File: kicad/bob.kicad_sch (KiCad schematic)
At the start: 49 parts, among them J1 GPIO (Optional), J2 Mini USB Female, J3 Battery Connector, J4 GPIO (Optional), SW1 Screw Switch, U1 RP2040, U2 W25Q64JVSS, U3 NCP1117-3.3_SOT223, U4 MPU-6050, Y1 12MHz

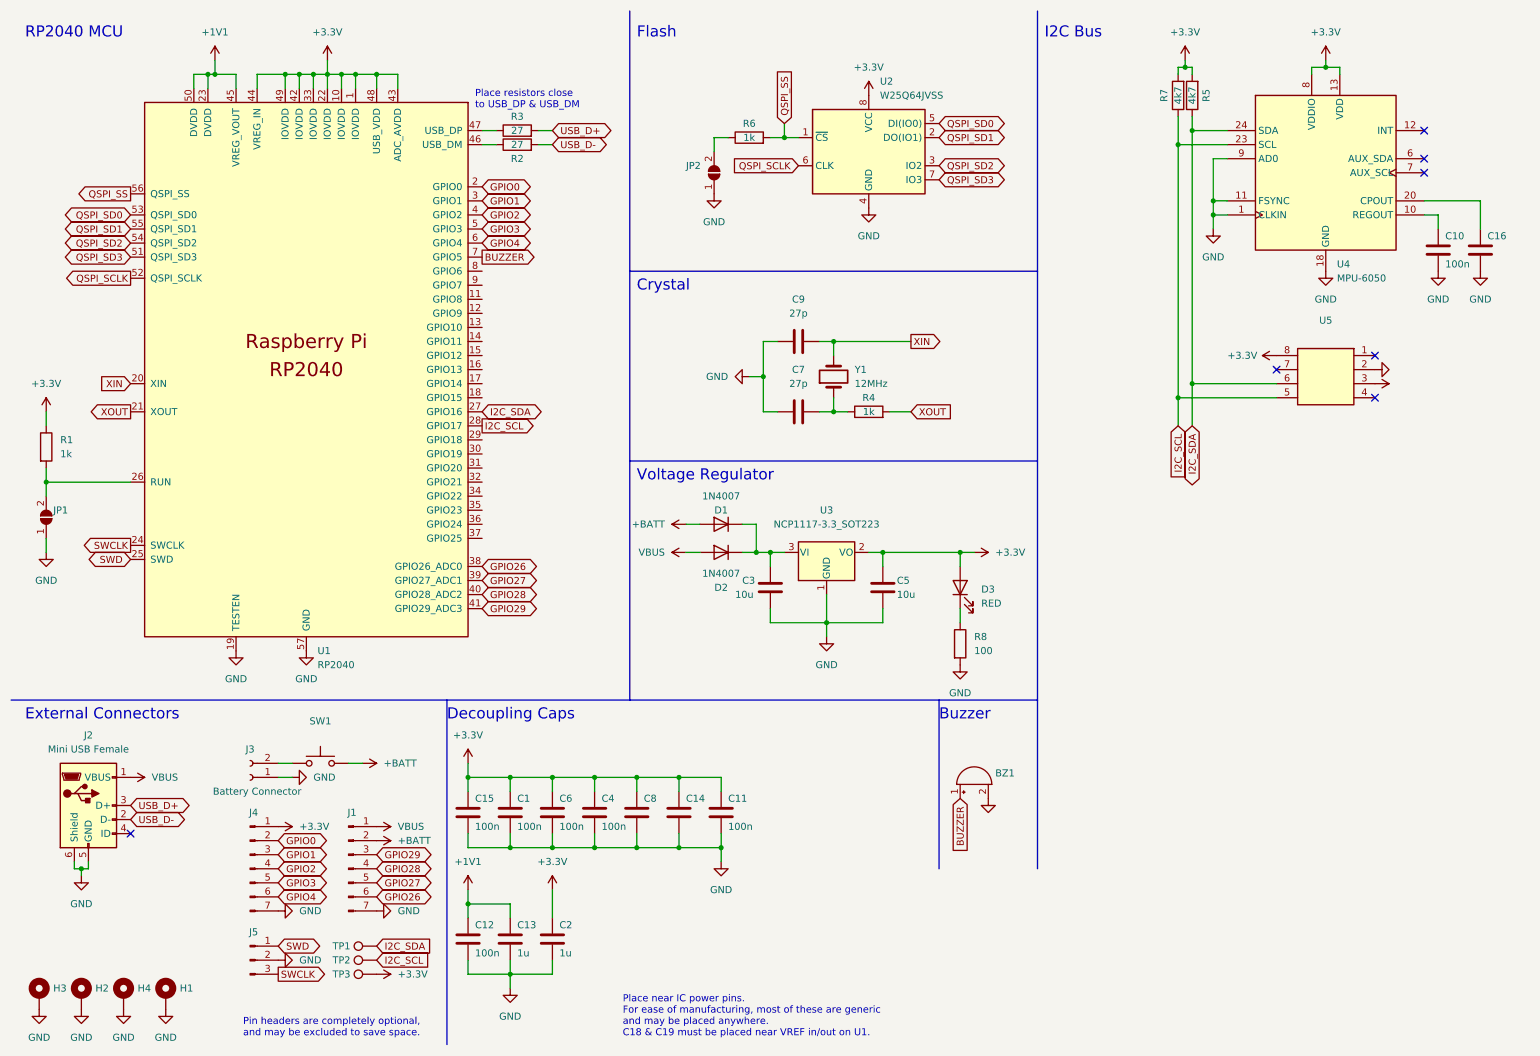
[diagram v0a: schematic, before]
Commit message: Added a magnetometer
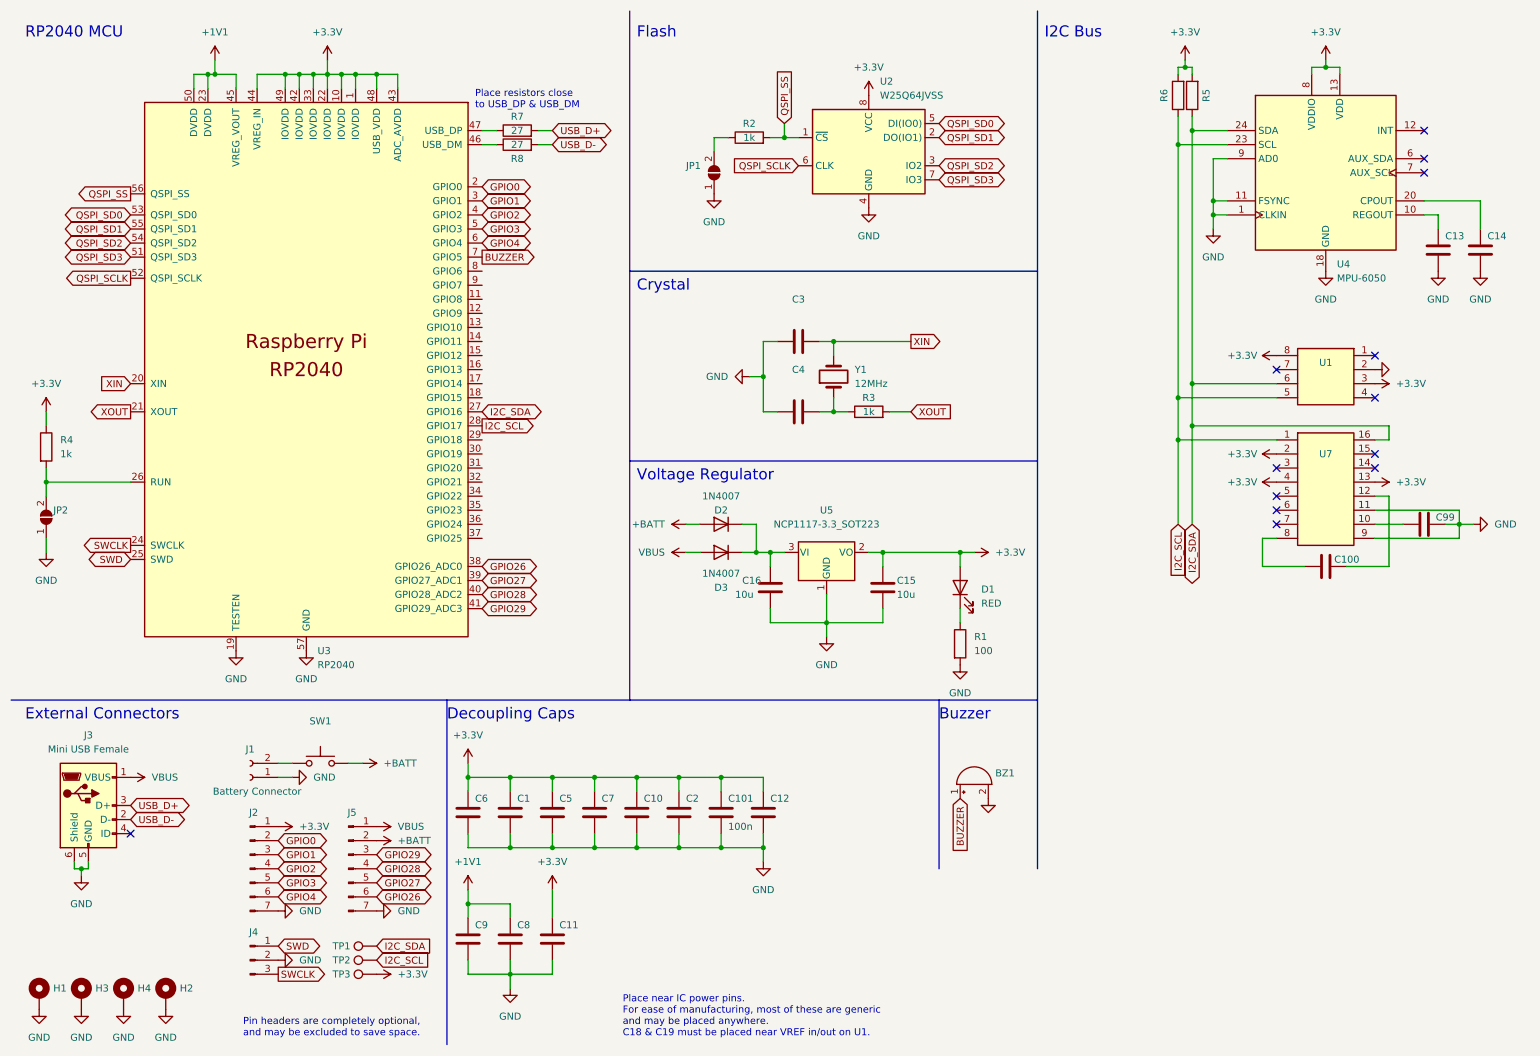
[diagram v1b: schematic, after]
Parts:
- added C100: (no value), Capacitor_SMD:C_0603_1608Metric, symbol Device:C
- added C101: 100n, Capacitor_SMD:C_0603_1608Metric, symbol Device:C
- added C99: (no value), symbol Device:C
- added U7: (no value), symbol IC_Generic:IC16
- C1: value 100n -> (none); LCSC (none) -> C14663
- C10: renamed from C8; LCSC (none) -> C14663
- C11: renamed from C2; value 1u -> (none); LCSC (none) -> C23969
- C12: renamed from C11; value 100n -> (none); LCSC (none) -> C14663
- C13: renamed from C10; value 100n -> (none); LCSC (none) -> C14663
- C2: renamed from C14; LCSC (none) -> C14663
- C3: renamed from C9; value 27p -> (none); LCSC (none) -> C730449
- C4: renamed from C7; value 27p -> (none); LCSC (none) -> C730449
- C5: renamed from C6; value 100n -> (none); LCSC (none) -> C14663
- C6: renamed from C15; value 100n -> (none); LCSC (none) -> C14663
- C7: renamed from C4; value 100n -> (none); LCSC (none) -> C14663
- C8: renamed from C13; value 1u -> (none); LCSC (none) -> C23969
- C9: renamed from C12; value 100n -> (none); LCSC (none) -> C14663
- J1: renamed from J3; footprint Connector_Wire:Compact_Relief -> Connector_Wire:2xRelief sideways
- J2: renamed from J4; footprint Connector_PinHeader_2.54mm:PinHeader_1x07_P2.54mm_Vertical -> Connector_PinHeader_2.54mm:PinHeader_1x07_P2.54mm_Vertical_NoSilk
- J5: renamed from J1; footprint Connector_PinHeader_2.54mm:PinHeader_1x07_P2.54mm_Vertical -> Connector_PinHeader_2.54mm:PinHeader_1x07_P2.54mm_Vertical_NoSilk
- R5: value 4k7 -> (none)
- R6: renamed from R7; value 4k7 -> (none)
- R7: renamed from R3; footprint (none) -> Resistor_SMD:R_0603_1608Metric_Pad0.98x0.95mm_HandSolder
- R8: renamed from R2; footprint (none) -> Resistor_SMD:R_0603_1608Metric_Pad0.98x0.95mm_HandSolder
- SW1: footprint Connector:Screw_Switch_M3 -> Connector:Screw_Switch_M2
- U3: renamed from U1; footprint RP2040_minimal:RP2040-QFN-56 -> RP2040_minimal:RP2040-QFN-56_HS
- U4: footprint Sensor_Motion:InvenSense_QFN-24_4x4mm_P0.5mm -> Sensor_Motion:InvenSense_QFN-24_4x4mm_P0.5mm_HS
- renumbered C16 to C14, C5 to C15, C3 to C16, D3 to D1, D1 to D2, D2 to D3, H3 to H1, H1 to H2, H2 to H3, J2 to J3, J5 to J4, JP2 to JP1, JP1 to JP2, R8 to R1, R6 to R2, R4 to R3, R1 to R4, U5 to U1, U3 to U5
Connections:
- net +3V3: now also C101.1, U7.13, U7.2, U7.4
- net GND: now also C101.2, C99.2, U7.11, U7.9
- net I2C_SCL: now also U7.1
- net I2C_SDA: now also U7.16
- new net: C100.1, U7.8
- new net: C100.2, U7.12
- new net: C99.1, U7.10
- no-connect marks 7 -> 13
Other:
- moved on the sheet: C12

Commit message: Rev 3, issued for production
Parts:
- removed C13, C14: (no value), symbol Device:C
- removed U4: MPU-6050, Sensor_Motion:InvenSense_QFN-24_4x4mm_P0.5mm_HS, symbol Sensor_Motion:MPU-6050
- added C15: (no value), symbol Device:C
- added TP4: (no value), symbol Connector:TestPoint
- added U5: (no value), symbol IC_Generic:IC14
- BZ1: JLC (none) -> DNF; LCSC (none) -> DNF
- C1: JLC (none) -> 0603
- C10: renamed from C3; JLC (none) -> 0603; LCSC C730449 -> C2312234
- C11: renamed from C9; JLC (none) -> 0603
- C12: renamed from C7; JLC (none) -> 0603
- C13: renamed from C4; JLC (none) -> 0603; LCSC C730449 -> C2312234
- C14: renamed from C101; value 100n -> (none); footprint Capacitor_SMD:C_0603_1608Metric -> (none); JLC (none) -> 0603
- C16: renamed from C99; JLC (none) -> 0603; LCSC (none) -> C19666
- C17: renamed from C100; footprint Capacitor_SMD:C_0603_1608Metric -> (none); JLC (none) -> 0603; LCSC (none) -> C21120
- C18: renamed from C2; JLC (none) -> 0603
- C2: renamed from C16; value 10u -> (none); footprint Capacitor_SMD:C_0603_1608Metric -> (none); JLC (none) -> 0603; LCSC (none) -> C96446
- C3: renamed from C11; JLC (none) -> 0603
- C4: renamed from C8; JLC (none) -> 0603
- C5: renamed from C12; JLC (none) -> 0603
- C6: renamed from C15; value 10u -> (none); footprint Capacitor_SMD:C_0603_1608Metric -> (none); JLC (none) -> 0603; LCSC (none) -> C96446
- C7: renamed from C5; JLC (none) -> 0603
- C8: renamed from C10; JLC (none) -> 0603
- C9: renamed from C6; JLC (none) -> 0603
- D1: renamed from D3; footprint Diode_SMD:D_SOD-123 -> (none); JLC (none) -> SOD-123FL; LCSC (none) -> C727081
- D2: footprint Diode_SMD:D_SOD-123 -> (none); JLC (none) -> SOD-123FL; LCSC (none) -> C727081
- D3: renamed from D1; value RED -> (none); footprint LED_THT:LED_D3.0mm -> (none); JLC (none) -> DNF; LCSC (none) -> DNF
- H1: renamed from H4; value MountingHole_Pad -> (none); footprint MountingHole:MountingHole_2.2mm_M2_DIN965_Pad -> (none); JLC (none) -> -; LCSC (none) -> -
- H2: renamed from H3; value MountingHole_Pad -> (none); footprint MountingHole:MountingHole_2.2mm_M2_DIN965_Pad -> (none); JLC (none) -> -; LCSC (none) -> -
- H3: renamed from H1; value MountingHole_Pad -> (none); footprint MountingHole:MountingHole_2.2mm_M2_DIN965_Pad -> (none); JLC (none) -> -; LCSC (none) -> -
- H4: renamed from H2; value MountingHole_Pad -> (none); footprint MountingHole:MountingHole_2.2mm_M2_DIN965_Pad -> (none); JLC (none) -> -; LCSC (none) -> -
- J1: renamed from J3; value Mini USB Female -> (none); footprint Connector_USB:USB_Mini-B_Lumberg_2486_01_Horizontal -> (none); JLC (none) -> SMD; LCSC (none) -> C2681563
- J2: renamed from J5; value GPIO (Optional) -> (none); footprint Connector_PinHeader_2.54mm:PinHeader_1x07_P2.54mm_Vertical_NoSilk -> (none); JLC (none) -> DNF; LCSC (none) -> DNF
- J3: renamed from J2; value GPIO (Optional) -> (none); footprint Connector_PinHeader_2.54mm:PinHeader_1x07_P2.54mm_Vertical_NoSilk -> (none); JLC (none) -> DNF; LCSC (none) -> DNF
- J4: renamed from J1; value Battery Connector -> (none); footprint Connector_Wire:2xRelief sideways -> (none); JLC (none) -> -; LCSC (none) -> -
- J5: renamed from J4; symbol Connector:Conn_01x03_Male -> Connector:Conn_01x02_Male; JLC (none) -> DNF; LCSC (none) -> DNF
- JP1, JP2: JLC (none) -> -; LCSC (none) -> -
- R1: renamed from R8; value 27 -> (none); footprint Resistor_SMD:R_0603_1608Metric_Pad0.98x0.95mm_HandSolder -> (none); JLC (none) -> 0603; LCSC (none) -> C25190
- R2: renamed from R7; value 27 -> (none); footprint Resistor_SMD:R_0603_1608Metric_Pad0.98x0.95mm_HandSolder -> (none); JLC (none) -> 0603; LCSC (none) -> C25190
- R3: renamed from R2; value 1k -> (none); JLC (none) -> 0603; LCSC (none) -> C21190
- R4: value 1k -> (none); JLC (none) -> 0603; LCSC (none) -> C21190
- R5: renamed from R3; value 1k -> (none); JLC (none) -> 0603; LCSC (none) -> C21190
- R6: renamed from R5; JLC (none) -> 0603; LCSC (none) -> C25804
- R7: renamed from R6; JLC (none) -> 0603; LCSC (none) -> C25804
- R8: renamed from R1; value 100 -> (none); JLC (none) -> 0603; LCSC (none) -> C22775
- SW1: value Screw Switch -> (none); footprint Connector:Screw_Switch_M2 -> (none); JLC (none) -> DNF; LCSC (none) -> DNF
- TP1: renamed from TP3; JLC (none) -> -; LCSC (none) -> -
- TP2: renamed from TP1; JLC (none) -> -; LCSC (none) -> -
- TP3: renamed from TP2; JLC (none) -> -; LCSC (none) -> -
- U1: renamed from U2; value W25Q64JVSS -> (none); footprint Package_SO:SOIC-8_5.23x5.23mm_P1.27mm -> (none); JLC (none) -> SOP-8_5.2x5.3x1.27P; LCSC (none) -> C83140
- U2: renamed from U5; value NCP1117-3.3_SOT223 -> (none); footprint Package_TO_SOT_SMD:SOT-223-3_TabPin2 -> (none); JLC (none) -> SOT-223; LCSC (none) -> C6186
- U3: value RP2040 -> (none); footprint RP2040_minimal:RP2040-QFN-56_HS -> (none); JLC (none) -> LQFN-56_EP_7.0x7.0x0.4P; LCSC (none) -> C2040
- U4: renamed from U7; JLC (none) -> LGA-16; LCSC (none) -> C976032
- U6: renamed from U1; JLC (none) -> LGA-8_3.6x3.8x0.9P; LCSC (none) -> C138665
- Y1: value 12MHz -> (none); footprint Crystal:Crystal_SMD_5032-2Pin_5.0x3.2mm -> (none); JLC (none) -> 5032; LCSC (none) -> C90884
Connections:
- net +3V3: now also C15.1, U5.12, U5.5, U5.8
- net GND: now also C15.2, TP4.1, U5.1, U5.2, U5.3, U5.6, U5.7; no longer J5.2 (Pin_2)
- net I2C_SCL: now also U5.13
- net I2C_SDA: now also U5.14
- net SWCLK: now also J5.2 (Pin_2); no longer J5.3 (Pin_3)
- no-connect marks 13 -> 14
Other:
- note added: "Place near IC power pins. For ease of manufacturing, most of these are generic and may be placed anywhere. 1u caps must be placed near VREF in/out on U1."
- note removed: "Place near IC power pins. For ease of manufacturing, most of these are generic and may be placed anywhere. C18 & C19 must be placed near VREF in/out on U1."
- moved on the sheet: C16, C17, C5, U4, U6
